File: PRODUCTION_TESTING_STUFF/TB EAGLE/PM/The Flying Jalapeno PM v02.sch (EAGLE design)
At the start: 8 parts

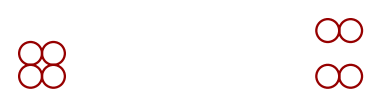
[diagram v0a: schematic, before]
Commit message: Added cutouts in the PM to allow space for nylon standoffs
had to mill these out on v01. Originally planned on testing without
these populated.
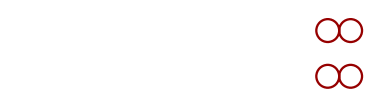
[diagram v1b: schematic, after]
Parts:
- removed STANDOFF1, STANDOFF2, STANDOFF3, STANDOFF4: STAND-OFFTIGHT, SparkFun-Electromechanical:STAND-OFFTIGHT
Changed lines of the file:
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@@
 <?xml version="1.0" encoding="utf-8"?>
 <!DOCTYPE eagle SYSTEM "eagle.dtd">
-<eagle version="7.3.0">
+<eagle version="7.6.0">
 <drawing>
 <settings>
@@
 </classes>
 <parts>
-<part name="STANDOFF1" library="SparkFun-Electromechanical" deviceset="STAND-OFF" device="TIGHT"/>
-<part name="STANDOFF2" library="SparkFun-Electromechanical" deviceset="STAND-OFF" device="TIGHT"/>
-<part name="STANDOFF3" library="SparkFun-Electromechanical" deviceset="STAND-OFF" device="TIGHT"/>
-<part name="STANDOFF4" library="SparkFun-Electromechanical" deviceset="STAND-OFF" device="TIGHT"/>
 <part name="STANDOFF5" library="SparkFun-Electromechanical" deviceset="STAND-OFF" device="TIGHT"/>
 <part name="STANDOFF6" library="SparkFun-Electromechanical" deviceset="STAND-OFF" device="TIGHT"/>
@@
 </plain>
 <instances>
-<instance part="STANDOFF1" gate="G$1" x="-22.86" y="7.62"/>
-<instance part="STANDOFF2" gate="G$1" x="-25.4" y="7.62"/>
-<instance part="STANDOFF3" gate="G$1" x="-22.86" y="10.16"/>
-<instance part="STANDOFF4" gate="G$1" x="-25.4" y="10.16"/>
 <instance part="STANDOFF5" gate="G$1" x="10.16" y="7.62"/>
 <instance part="STANDOFF6" gate="G$1" x="7.62" y="7.62"/>
